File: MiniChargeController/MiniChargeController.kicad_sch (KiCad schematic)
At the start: 41 parts, among them J1 Screw_Terminal_01x02, Q1 AO3400A, Q2 AO3400A, Q3 AO3400A, Q4 AO3400A, Q5 AO3401A, U1 BQ25798RQMR, U2 ATTINY20-SSU_C614835

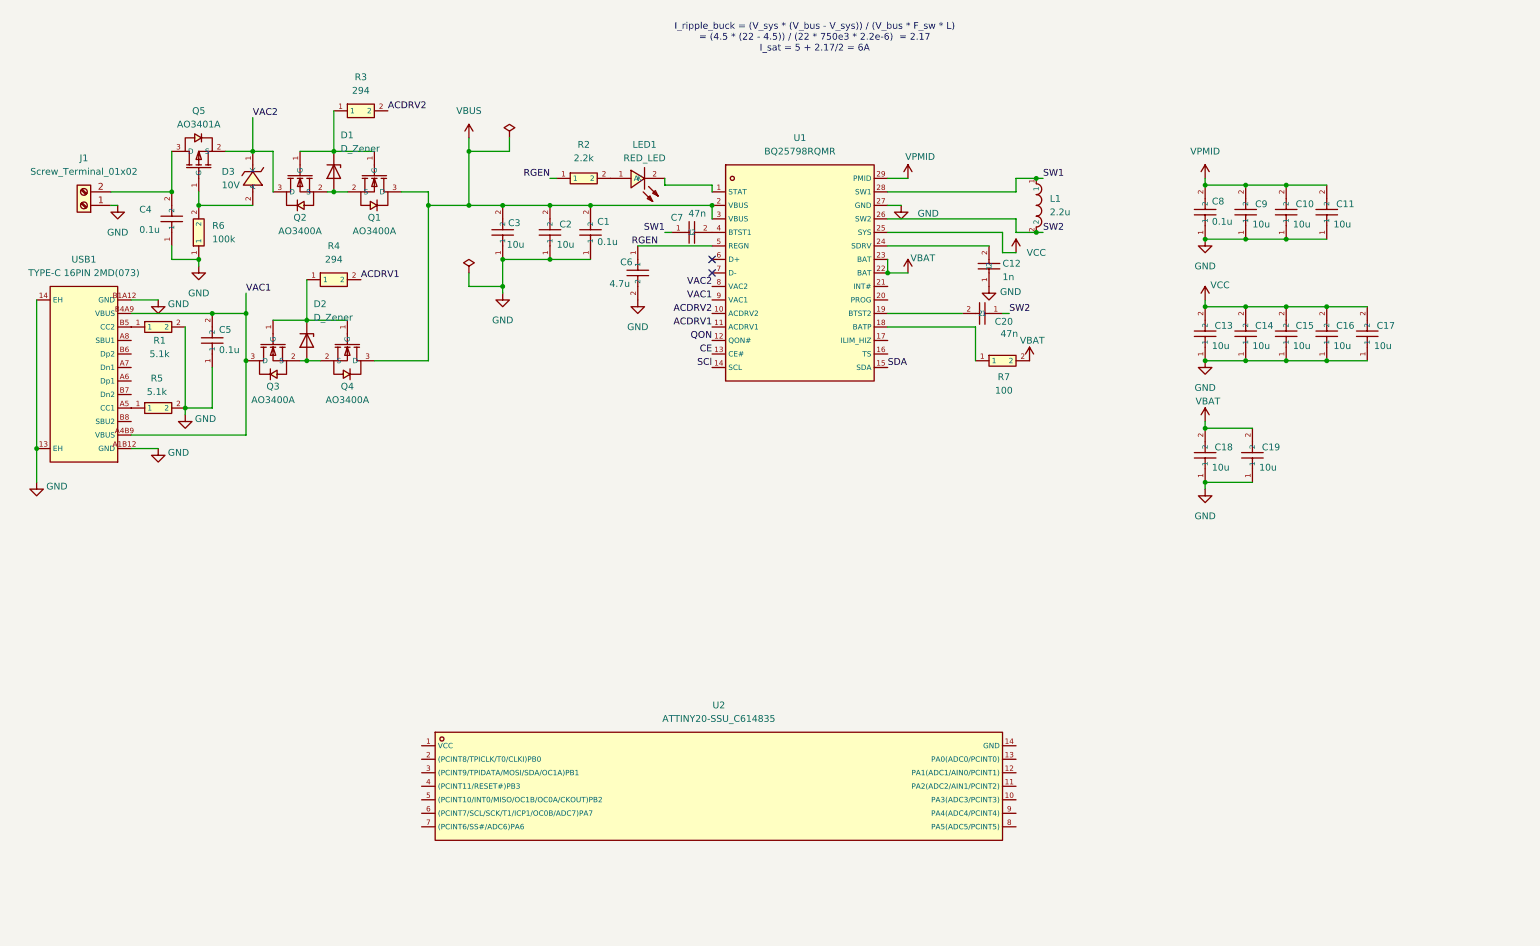
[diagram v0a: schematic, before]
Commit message: Mostly finished schematic, need to finish wiring battery and revalidate schematic
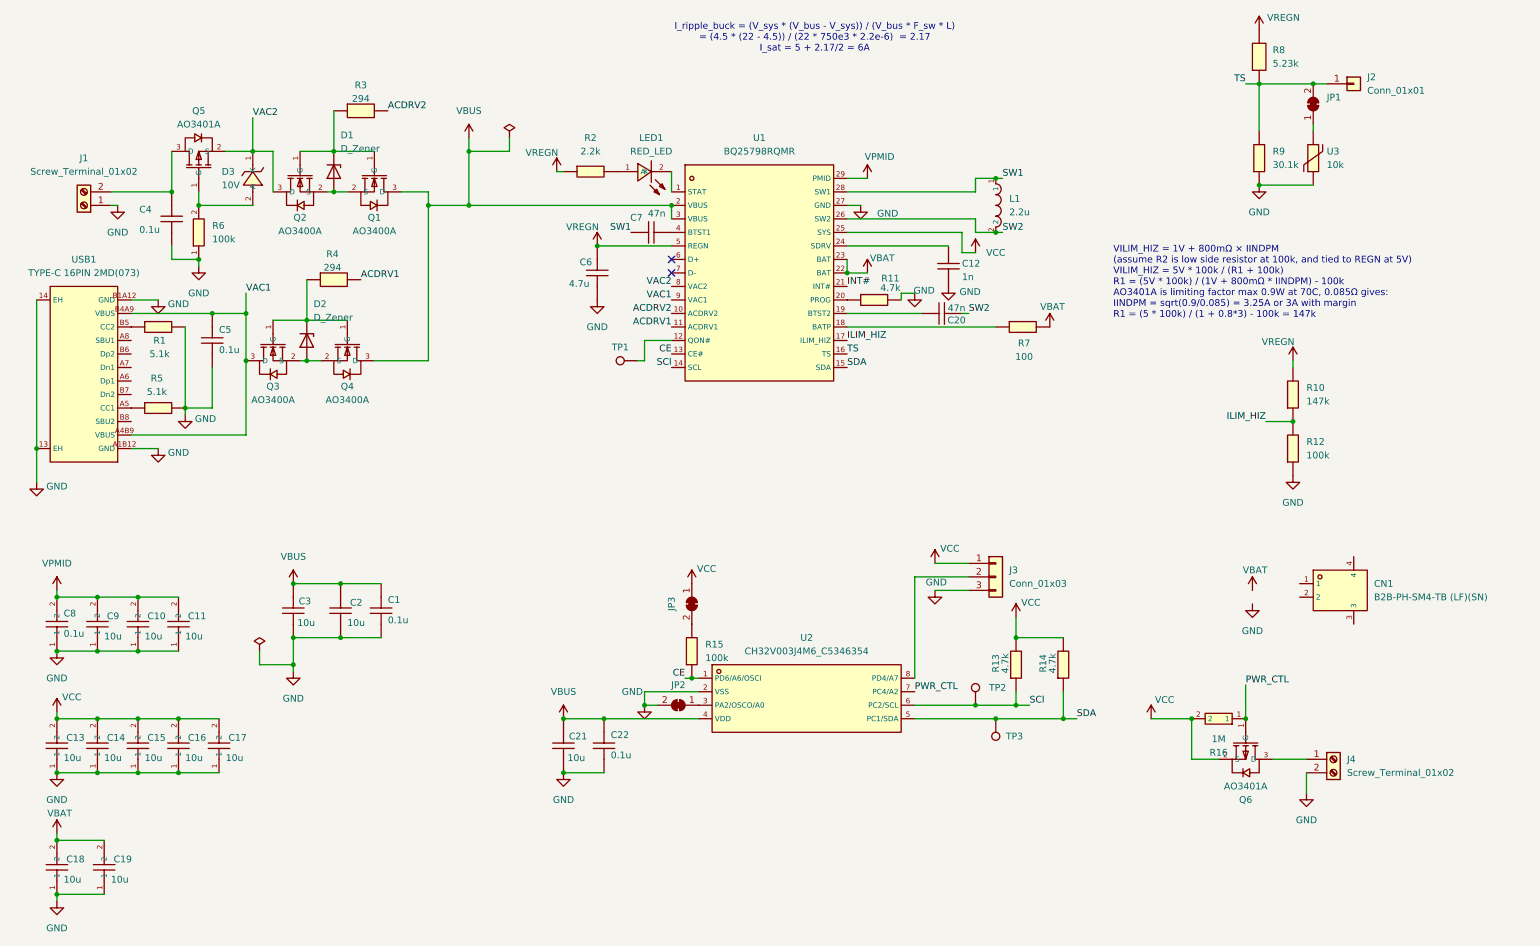
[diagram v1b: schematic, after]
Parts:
- removed U2: ATTINY20-SSU_C614835, lcsc_footprints:C614835_SOIC-14_L8_7-W3_9-P1_27-LS6_0-BL, symbol lcsc_imported:ATTINY20-SSU_C614835
- added C21: 10u, lcsc_footprints:C440198_C0805, symbol lcsc_imported:GRM21BR61H106KE43L
- added C22: 0.1u, lcsc_footprints:C1525_C0402, symbol lcsc_imported:100nF_(104)_±10%_16V
- added CN1: B2B-PH-SM4-TB (LF)(SN), lcsc_footprints:C160352_CONN-SMD_B2B-PH-SM4-TB-LF-SN, symbol lcsc_imported:B2B-PH-SM4-TB_(LF)(SN)
- added J2: Conn_01x01, Connector_PinHeader_2.54mm:PinHeader_1x01_P2.54mm_Vertical, symbol Connector_Generic:Conn_01x01
- added J3: Conn_01x03, Connector_PinHeader_2.54mm:PinHeader_1x03_P2.54mm_Vertical, symbol Connector_Generic:Conn_01x03
- added J4: Screw_Terminal_01x02, Package_TO_SOT_THT:TO-46-3, symbol Connector:Screw_Terminal_01x02
- added JP1, JP2, JP3: (no value), Jumper:SolderJumper-2_P1.3mm_Bridged_RoundedPad1.0x1.5mm, symbol Jumper:SolderJumper_2_Bridged
- added Q6: AO3401A, lcsc_footprints:C15127_SOT-23_L2_9-W1_3-P1_90-LS2_4-BR, symbol lcsc_imported:AO3401A
- added R10: 147k, lcsc_footprints:C163489_R0402, symbol lcsc_imported:RC0402FR-07147KL
- added R11, R13, R14: 4.7k, lcsc_footprints:C25900_R0402, symbol lcsc_imported:4_7KΩ_(4701)_±1%
- added R12, R15: 100k, lcsc_footprints:C25741_R0402, symbol lcsc_imported:100KΩ_(1003)_±1%
- added R16: 1M, lcsc_footprints:C26083_R0402, symbol lcsc_imported:1MΩ_(1004)_±1%
- added R8: 5.23k, lcsc_footprints:C2933105_R0402, symbol lcsc_imported:FRC0402F5231TS
- added R9: 30.1k, lcsc_footprints:C29402_R0402, symbol lcsc_imported:30_1KΩ_(3012)_±1%
- added TP1, TP2, TP3: TestPoint, TestPoint:TestPoint_Pad_D1.0mm, symbol Connector:TestPoint
- added U2: CH32V003J4M6_C5346354, lcsc_footprints:C5346354_SOP-8_L4_9-W3_8-P1_27-LS6_0-BL, symbol lcsc_imported:CH32V003J4M6_C5346354
- added U3: 10k, lcsc_footprints:C5121989_R0402, symbol lcsc_imported:NTCG103JF103FT1S
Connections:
- net CE: now also R15.1, U2.1 (PD6/A6/OSCI)
- net GND: now also C21.1, C22.1, J3.3 (Pin_3), J4.2 (Pin_2), JP2.2 (B), R11.2, R12.1, R9.1, U2.2 (VSS), U3.1
- net SCl: now also R13.1, TP2.1, U2.6 (PC2/SCL)
- net SDA: now also R14.1, TP3.1, U2.5 (PC1/SDA)
- net VBUS: now also C21.2, C22.2, U2.4 (VDD)
- net VCC: now also J3.1 (Pin_1), JP3.1 (A), Q6.2 (S), R13.2, R14.2, R16.2
- net TS: now reaches U1.16 (TS)
- net TS: now also J2.1 (Pin_1), JP1.2 (B), R8.1, R9.2
- net ILIM_HIZ: now reaches U1.17 (ILIM_HIZ)
- net ILIM_HIZ: now also R10.1, R12.2
- net at U1.20 (PROG): now also R11.1
- net INT#: now reaches U1.21 (INT#)
- net QON: no longer names the net of U1.12 (QON#)
- net QON: now also TP1.1
- net RGEN renamed VREGN
- net VREGN: now also R10.2, R8.2
- new net: JP2.1 (A), U2.3 (PA2/OSCO/A0)
- new net: J3.2 (Pin_2), U2.8 (PD4/A7)
- new net: J4.1 (Pin_1), Q6.3 (D)
- new net: JP3.2 (B), R15.2
- new net: JP1.1 (A), U3.2
- new net PWR_CTL: Q6.1 (G), R16.1, U2.7 (PC4/A2)
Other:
- note added: "VILIM_HIZ = 1V + 800mΩ × IINDPM (assume R2 is low side resistor at 100k, and tied to REGN at 5V) VILIM_HIZ = 5V * 100k / (R1 + 100k) R1 = (5V * 100k) / (1V + 800mΩ * IINDPM) - 100k AO3401A is limiting factor max 0.9W at 70C, 0.085Ω gives: IINDPM = sqrt(0.9/0.085) = 3.25A or 3A with margin R1 = (5 * 100k) / (1 + 0.8*3) - 100k = 147k"
- moved on the sheet: C10, C11, C13, C14, C15, C16, C17, C18, C19, C8, C9, L1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

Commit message: Added battery connector
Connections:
- net GND: now also CN1.2, CN1.3, CN1.4
- net VBAT: now also CN1.1
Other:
- moved on the sheet: CN1
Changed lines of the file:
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@@
 	(wire
 		(pts
+			(xy 237.49 119.38) (xy 240.03 119.38)
+		)
+		(stroke
+			(width 0)
+			(type default)
+		)
+	)
+	(wire
+		(pts
 			(xy 19.05 121.92) (xy 19.05 123.19)
 		)
@@
 	(wire
 		(pts
+			(xy 250.19 114.3) (xy 254 114.3)
+		)
+		(stroke
+			(width 0)
+			(type default)
+		)
+	)
+	(wire
+		(pts
 			(xy 196.85 44.45) (xy 195.58 44.45)
 		)
@@
 	(wire
 		(pts
+			(xy 237.49 121.92) (xy 240.03 121.92)
+		)
+		(stroke
+			(width 0)
+			(type default)
+		)
+	)
+	(wire
+		(pts
 			(xy 129.54 143.51) (xy 132.08 143.51)
 		)
@@
 	(symbol
 		(lib_id "lcsc_imported:B2B-PH-SM4-TB_(LF)(SN)")
-		(at 259.08 121.92 0)
+		(at 246.38 120.65 0)
 		(unit 1)
 		(body_style 1)
@@
 		(fields_autoplaced yes)
 		(property "Reference" "CN1"
-			(at 266.7 120.6499 0)
+			(at 254 119.3799 0)
 			(show_name no)
 			(do_not_autoplace no)
@@
 		)
 		(property "Value" "B2B-PH-SM4-TB (LF)(SN)"
-			(at 266.7 123.1899 0)
+			(at 254 121.9199 0)
 			(show_name no)
 			(do_not_autoplace no)
@@
 		)
 		(property "Footprint" "lcsc_footprints:C160352_CONN-SMD_B2B-PH-SM4-TB-LF-SN"
-			(at 259.08 132.08 0)
+			(at 246.38 130.81 0)
 			(hide yes)
 			(show_name no)
@@
 		)
 		(property "Datasheet" "https://www.lcsc.com/datasheet/lcsc_datasheet_2304140030_JST-B2B-PH-SM4-TB-LF-SN_C160352.pdf"
-			(at 256.794 121.793 0)
+			(at 244.094 120.523 0)
 			(hide yes)
 			(show_name no)
@@
 		)
 		(property "Description" "B2B-PH-SM4-TB (LF)(SN)"
-			(at 259.08 121.92 0)
+			(at 246.38 120.65 0)
 			(hide yes)
 			(show_name no)
@@
 		)
 		(property "LCSC" "C160352"
-			(at 259.08 121.92 0)
+			(at 246.38 120.65 0)
 			(hide yes)
 			(show_name no)
@@
 		)
 		(property "Manufacturer" "JST"
-			(at 259.08 121.92 0)
+			(at 246.38 120.65 0)
 			(hide yes)
 			(show_name no)
@@
 	(symbol
 		(lib_id "power:GND")
-		(at 243.84 124.46 0)
+		(at 237.49 121.92 0)
 		(unit 1)
 		(body_style 1)
@@
 		(fields_autoplaced yes)
 		(property "Reference" "#PWR040"
-			(at 243.84 130.81 0)
+			(at 237.49 128.27 0)
 			(hide yes)
 			(show_name no)
@@
 		)
 		(property "Value" "GND"
-			(at 243.84 129.54 0)
+			(at 237.49 127 0)
 			(show_name no)
 			(do_not_autoplace no)
@@
 		)
 		(property "Footprint" "lcsc_footprints:C377773_C0805"
-			(at 243.84 124.46 0)
+			(at 237.49 121.92 0)
 			(hide yes)
 			(show_name no)
@@
 		)
 		(property "Datasheet" ""
-			(at 243.84 124.46 0)
+			(at 237.49 121.92 0)
 			(hide yes)
 			(show_name no)
@@
 		)
 		(property "Description" "Power symbol creates a global label with name \"GND\" , ground"
-			(at 243.84 124.46 0)
+			(at 237.49 121.92 0)
 			(hide yes)
 			(show_name no)
@@
 	)
 	(symbol
+		(lib_id "power:GND")
+		(at 254 114.3 0)
+		(unit 1)
+		(body_style 1)
+		(exclude_from_sim no)
+		(in_bom yes)
+		(on_board yes)
+		(in_pos_files yes)
+		(dnp no)
+		(property "Reference" "#PWR042"
+			(at 254 120.65 0)
+			(hide yes)
+			(show_name no)
+			(do_not_autoplace no)
+			(effects
+				(font
+					(size 1.27 1.27)
+				)
+			)
+		)
+		(property "Value" "GND"
+			(at 258.572 114.554 0)
+			(show_name no)
+			(do_not_autoplace no)
+			(effects
+				(font
+					(size 1.27 1.27)
+				)
+			)
+		)
+		(property "Footprint" "lcsc_footprints:C377773_C0805"
+			(at 254 114.3 0)
+			(hide yes)
+			(show_name no)
+			(do_not_autoplace no)
+			(effects
+				(font
+					(size 1.27 1.27)
+				)
+			)
+		)
+		(property "Datasheet" ""
+			(at 254 114.3 0)
+			(hide yes)
+			(show_name no)
+			(do_not_autoplace no)
+			(effects
+				(font
+					(size 1.27 1.27)
+				)
+			)
+		)
+		(property "Description" "Power symbol creates a global label with name \"GND\" , ground"
+			(at 254 114.3 0)
+			(hide yes)
+			(show_name no)
+			(do_not_autoplace no)
+			(effects
+				(font
+					(size 1.27 1.27)
+				)
+			)
+		)
+		(pin "1"
+		)
+		(instances
+			(project "MiniChargeController"
+				(path "/b35b4552-f45c-4b02-b546-1657edfbb5c4"
+					(reference "#PWR042")
+					(unit 1)
+				)
+			)
+		)
+	)
+	(symbol
 		(lib_id "lcsc_imported:GRM21BR61H106KE43L")
 		(at 49.53 151.13 90)
@@
 	(symbol
 		(lib_id "power:VCC")
-		(at 243.84 121.92 0)
+		(at 237.49 119.38 0)
 		(unit 1)
 		(body_style 1)
@@
 		(dnp no)
 		(property "Reference" "#PWR039"
-			(at 243.84 125.73 0)
+			(at 237.49 123.19 0)
 			(hide yes)
 			(show_name no)
@@
 		)
 		(property "Value" "VBAT"
-			(at 244.348 118.11 0)
+			(at 237.998 115.57 0)
 			(show_name no)
 			(do_not_autoplace no)
@@
 		)
 		(property "Footprint" "Sensor_Humidity:Sensirion_DFN-4_1.5x1.5mm_P0.8mm_SHT4x_NoCentralPad"
-			(at 243.84 121.92 0)
+			(at 237.49 119.38 0)
 			(hide yes)
 			(show_name no)
@@
 		)
 		(property "Datasheet" ""
-			(at 243.84 121.92 0)
+			(at 237.49 119.38 0)
 			(hide yes)
 			(show_name no)
@@
 		)
 		(property "Description" "Power symbol creates a global label with name \"VCC\""
-			(at 243.84 121.92 0)
+			(at 237.49 119.38 0)
 			(hide yes)
 			(show_name no)
@@
 					(unit 1)
 				)
+			)
+		)
+	)
+	(symbol
+		(lib_id "power:GND")
+		(at 250.19 127 0)
+		(unit 1)
+		(body_style 1)
+		(exclude_from_sim no)
+		(in_bom yes)
+		(on_board yes)
+		(in_pos_files yes)
+		(dnp no)
+		(fields_autoplaced yes)
+		(property "Reference" "#PWR041"
+			(at 250.19 133.35 0)
+			(hide yes)
+			(show_name no)
+			(do_not_autoplace no)
+			(effects
+				(font
+					(size 1.27 1.27)
+				)
+			)
+		)
+		(property "Value" "GND"
+			(at 250.19 132.08 0)
+			(show_name no)
+			(do_not_autoplace no)
+			(effects
+				(font
+					(size 1.27 1.27)
+				)
+			)
+		)
+		(property "Footprint" "lcsc_footprints:C377773_C0805"
+			(at 250.19 127 0)
+			(hide yes)
+			(show_name no)
+			(do_not_autoplace no)
+			(effects
+				(font
+					(size 1.27 1.27)
+				)
+			)
+		)
+		(property "Datasheet" ""
+			(at 250.19 127 0)
+			(hide yes)
+			(show_name no)
+			(do_not_autoplace no)
+			(effects
+				(font
+					(size 1.27 1.27)
+				)
+			)
+		)
+		(property "Description" "Power symbol creates a global label with name \"GND\" , ground"
+			(at 250.19 127 0)
+			(hide yes)
+			(show_name no)
+			(do_not_autoplace no)
+			(effects
+				(font
+					(size 1.27 1.27)
+				)
+			)
+		)
+		(pin "1"
+		)
+		(instances
+			(project "MiniChargeController"
+				(path "/b35b4552-f45c-4b02-b546-1657edfbb5c4"
+					(reference "#PWR041")
+					(unit 1)
+				)

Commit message: Replaced expensive caps, swapped out charge controller for cheaper variant
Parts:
- removed C10, C11, C13, C14, C15, C16, C17, C18, C19, C2, C21, C3, C9: 10u, lcsc_footprints:C440198_C0805, symbol lcsc_imported:GRM21BR61H106KE43L
- removed J2: Conn_01x01, Connector_PinHeader_2.54mm:PinHeader_1x01_P2.54mm_Vertical, symbol Connector_Generic:Conn_01x01
- removed JP2: (no value), Jumper:SolderJumper-2_P1.3mm_Bridged_RoundedPad1.0x1.5mm, symbol Jumper:SolderJumper_2_Bridged
- removed U1: BQ25798RQMR, lcsc_footprints:C2876593_QFN-29_L4_0-W4_0-P0_40-TL-BQ25792RQMR, symbol lcsc_imported:BQ25798RQMR
- added C13, C14, C15, C16, C17, C2, C21, C3: 10u, lcsc_footprints:C19702_C0603, symbol lcsc_imported:CL10A106KP8NNNC
- added C23: 10n, lcsc_footprints:C15195_C0402, symbol lcsc_imported:10nF_(103)_±10%_50V
- added J2: Conn_01x02, lcsc_footprints:C2862876_QFN-29_L4_0-W4_0-P0_40-TL-BQ25792RQMR, symbol Connector_Generic:Conn_01x02
- added R17, R19: 100k, lcsc_footprints:C25741_R0402, symbol lcsc_imported:100KΩ_(1003)_±1%
- added R18: 10k, lcsc_footprints:C25744_R0402, symbol lcsc_imported:10KΩ_(1002)_±1%
- added U1, U5, U6, U7, U8: 10u 35V, lcsc_footprints:C22367827_C0603, symbol lcsc_imported:HGC0603R5106M350NTHJ
- added U4: BQ25792RQMR, lcsc_footprints:C2862876_QFN-29_L4_0-W4_0-P0_40-TL-BQ25792RQMR, symbol lcsc_imported:BQ25792RQMR
- J1, J4: footprint Package_TO_SOT_THT:TO-46-3 -> TerminalBlock:TerminalBlock_Xinya_XY308-2.54-2P_1x02_P2.54mm_Horizontal
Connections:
- net ACDRV1: now also U4.11 (ACDRV1)
- net ACDRV2: now also U4.10 (ACDRV2)
- net CE: now also U4.13 (CE#)
- net GND: now also C13.1, C14.1, C15.1, C16.1, C17.1, C2.1, C21.1, C23.1, C3.1, J2.2 (Pin_2), U1.1, U4.27 (GND), U5.1, U6.1, U7.1, U8.1
- net ILIM_HIZ: now also U4.17 (ILIM_HIZ)
- net INT#: now also R18.1, R19.2, U4.21 (INT#)
- net PWR_CTL: now also R17.2; no longer Q6.1 (G), R16.1
- net SCl: now also U4.14 (SCL)
- net SDA: now also U4.15 (SDA)
- net SW1: now also U4.28 (SW1)
- net SW2: now also U4.26 (SW2)
- net TS: now also J2.1 (Pin_1), U4.16 (TS)
- net VAC1: now also U4.9 (VAC1)
- net VAC2: now also U4.8 (VAC2)
- net VBAT: now also C16.2, C17.2, U4.22 (BAT), U4.23 (BAT)
- net VBUS: now also U1.2, U4.2 (VBUS), U4.3 (VBUS), U5.2; no longer C22.2, U2.4 (VDD)
- net VCC: now also C22.2, U2.4 (VDD), C13.2, C14.2, C15.2, C2.2, C21.2, C3.2, R19.1, U4.25 (SYS)
- net VPMID: now also U4.29 (PMID), U6.2, U7.2, U8.2
- net VREGN: now also U4.5 (REGN)
- net at U2.3 (PA2/OSCO/A0): now also R18.2
- net at TP1.1: now also U4.12 (QON#)
- net at C20.2: now also U4.19 (BTST2)
- net at R7.1: now also U4.18 (BATP)
- net at C12.2: now also U4.24 (SDRV)
- net at LED1.2 (K): now also U4.1 (STAT)
- net at R11.1: now also U4.20 (PROG)
- net at C7.2: now also U4.4 (BTST1)
- new net: C23.2, Q6.1 (G), R16.1, R17.1
- no-connect marks 2 -> 8
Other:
- moved on the sheet: C12, C20, C22, CN1, J3, JP3, L1, R10, R11, R12, R13, R14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
